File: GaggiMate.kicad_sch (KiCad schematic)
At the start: 39 parts, among them J1 Heater SSR, J10 Analog sensors, J12 BTNS, J2 Conn_01x02, J3 K-Type probe, J4 Conn_01x02, J5 Pressure Sensor, J6 Conn_01x10_Pin, J8 Conn_01x12_Pin, J9 HX711 connector, P1 USB_C_Plug_USB2.0, U1 ESP32-S3-WROOM-1, U2 MAX31855KASA, U3 ADS1115IDGS, U4 AMS1117-3.3, U5 USBLC6-2P6

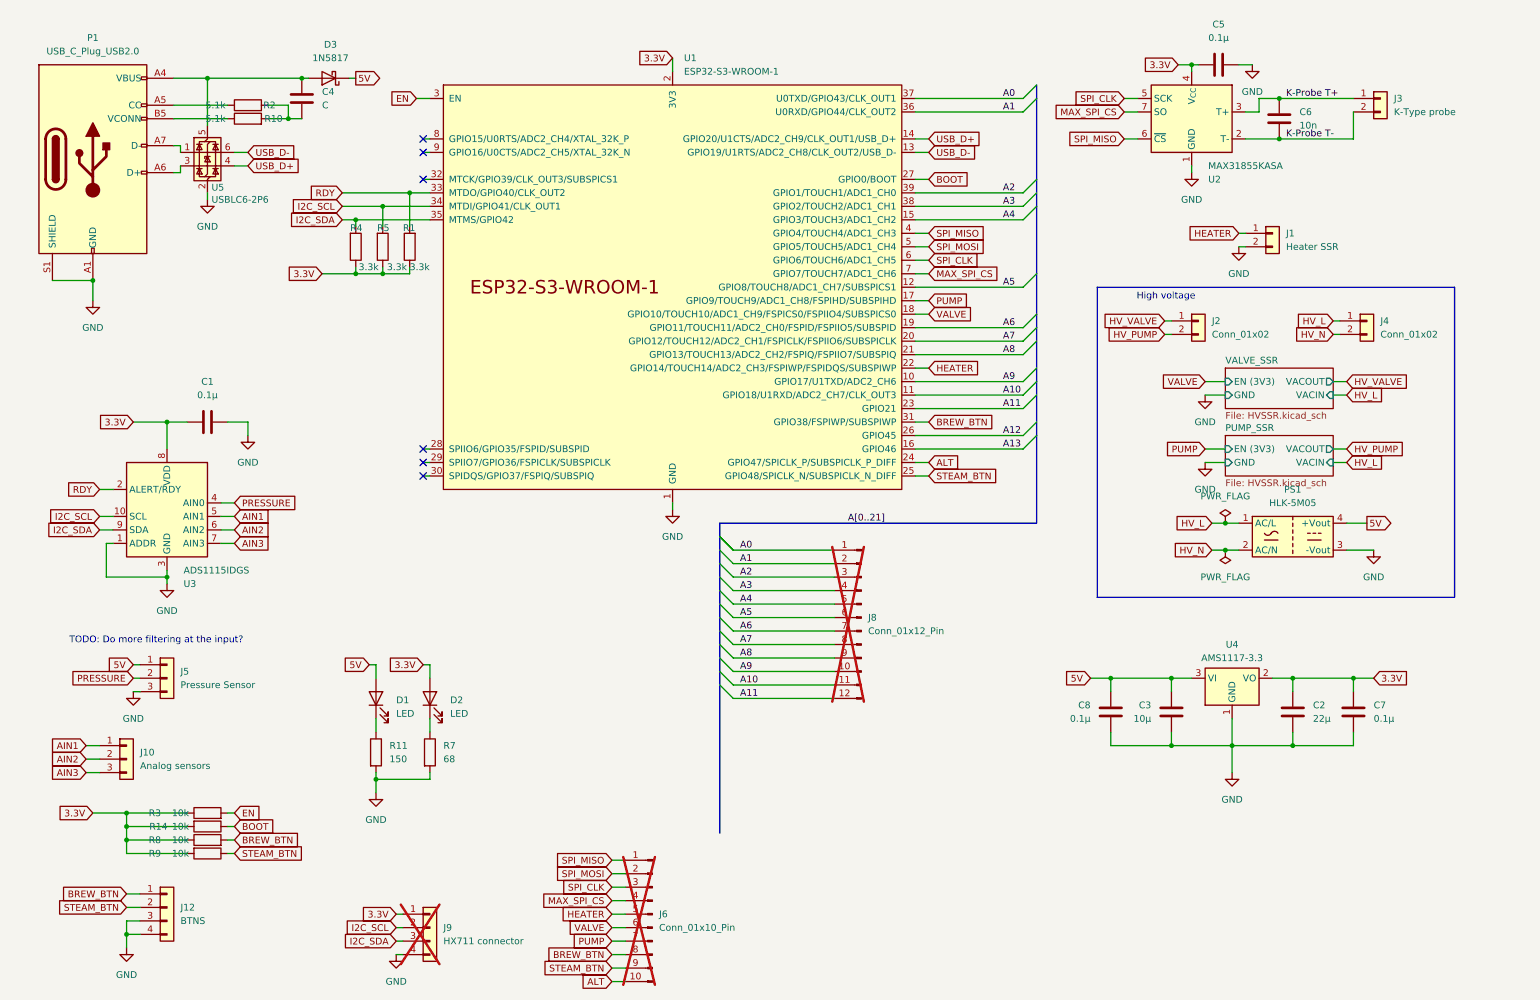
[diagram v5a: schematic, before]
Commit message: Moved front side components to other board, finished cap and resistor selection and maybe finalizing layout
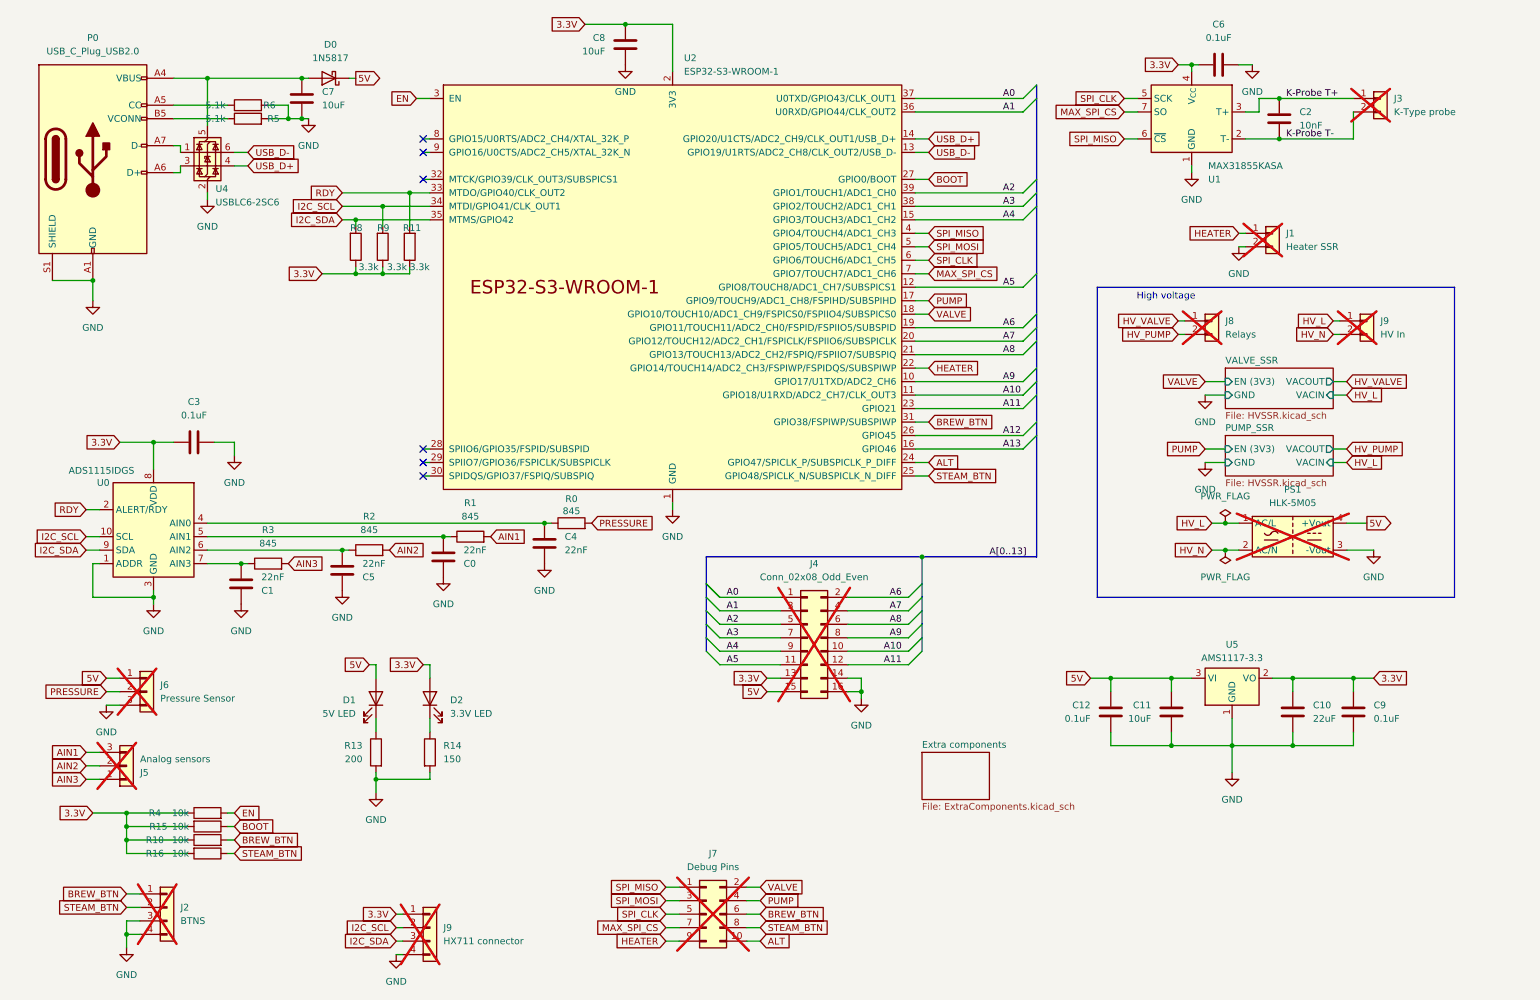
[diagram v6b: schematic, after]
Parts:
- removed J6: Conn_01x10_Pin, symbol Connector:Conn_01x10_Pin
- removed J8: Conn_01x12_Pin, Connector_PinHeader_2.54mm:PinHeader_1x12_P2.54mm_Vertical_SMD_Pin1Left, symbol Connector:Conn_01x12_Pin
- removed U5: USBLC6-2P6, Package_TO_SOT_SMD:SOT-666, symbol Power_Protection:USBLC6-2P6
- added C0, C1, C5: 22nF, Capacitor_SMD:C_0603_1608Metric, symbol Device:C
- added C7, C8: 10uF, Capacitor_SMD:C_0603_1608Metric, symbol Device:C
- added J4: Conn_02x08_Odd_Even, Connector_PinHeader_2.54mm:PinHeader_2x08_P2.54mm_Vertical_SMD, symbol Connector_Generic:Conn_02x08_Odd_Even
- added J7: Debug Pins, Connector_PinHeader_2.54mm:PinHeader_2x05_P2.54mm_Vertical_SMD, symbol Connector_Generic:Conn_02x05_Odd_Even
- added R0, R1, R2, R3: 845, Resistor_SMD:R_0603_1608Metric, symbol Device:R
- added U4: USBLC6-2SC6, Package_TO_SOT_SMD:SOT-23-6, symbol Power_Protection:USBLC6-2SC6
- C10: renamed from C2; value 22µ -> 22uF; footprint Capacitor_SMD:C_0201_0603Metric -> Capacitor_SMD:C_0603_1608Metric
- C11: renamed from C3; value 10µ -> 10uF; footprint Capacitor_SMD:C_0201_0603Metric -> Capacitor_SMD:C_0603_1608Metric
- C12: renamed from C8; value 0.1µ -> 0.1uF; footprint Capacitor_SMD:C_0201_0603Metric -> Capacitor_SMD:C_0603_1608Metric
- C2: renamed from C6; value 10n -> 10nF; footprint (none) -> Capacitor_SMD:C_0603_1608Metric
- C3: renamed from C1; value 0.1µ -> 0.1uF; footprint Capacitor_SMD:C_0201_0603Metric -> Capacitor_SMD:C_0603_1608Metric
- C4: value C -> 22nF; footprint Capacitor_SMD:C_0201_0603Metric -> Capacitor_SMD:C_0603_1608Metric
- C6: renamed from C5; value 0.1µ -> 0.1uF; footprint (none) -> Capacitor_SMD:C_0603_1608Metric
- C9: renamed from C7; value 0.1µ -> 0.1uF; footprint Capacitor_SMD:C_0201_0603Metric -> Capacitor_SMD:C_0603_1608Metric
- D1: value LED -> 5V LED; footprint (none) -> LED_SMD:LED_0603_1608Metric
- D2: value LED -> 3.3V LED; footprint (none) -> LED_SMD:LED_0603_1608Metric
- J1, J3: now not fitted
- J2: renamed from J12; now not fitted
- J5: renamed from J10; now not fitted
- J6: renamed from J5; now not fitted
- J8: renamed from J2; value Conn_01x02 -> Relays; now not fitted; now in the parts list
- J9: renamed from J4; value Conn_01x02 -> HV In; now not fitted; now in the parts list
- PS1: now not fitted; now in the parts list
- R10: renamed from R8; footprint Resistor_SMD:R_0201_0603Metric -> Resistor_SMD:R_0603_1608Metric
- R11: renamed from R1; footprint Resistor_SMD:R_0201_0603Metric -> Resistor_SMD:R_0603_1608Metric
- R13: renamed from R11; value 150 -> 200; footprint Resistor_SMD:R_0201_0603Metric -> Resistor_SMD:R_0603_1608Metric
- R14: renamed from R7; value 68 -> 150; footprint Resistor_SMD:R_0201_0603Metric -> Resistor_SMD:R_0603_1608Metric
- R15: renamed from R14; footprint Resistor_SMD:R_0201_0603Metric -> Resistor_SMD:R_0603_1608Metric
- R16: renamed from R9; footprint Resistor_SMD:R_0201_0603Metric -> Resistor_SMD:R_0603_1608Metric
- R4: renamed from R3; footprint Resistor_SMD:R_0201_0603Metric -> Resistor_SMD:R_0603_1608Metric
- R5: renamed from R10; footprint Resistor_SMD:R_0201_0603Metric -> Resistor_SMD:R_0603_1608Metric
- R6: renamed from R2; footprint Resistor_SMD:R_0201_0603Metric -> Resistor_SMD:R_0603_1608Metric
- R8: renamed from R4; footprint Resistor_SMD:R_0201_0603Metric -> Resistor_SMD:R_0603_1608Metric
- R9: renamed from R5; footprint Resistor_SMD:R_0201_0603Metric -> Resistor_SMD:R_0603_1608Metric
- renumbered D3 to D0, P1 to P0, U3 to U0, U2 to U1, U1 to U2, U4 to U5
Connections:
- net 3.3V: now also C8.2, J4.13 (Pin_13)
- net 5V: now also J4.15 (Pin_15)
- net A0: now also J4.1 (Pin_1)
- net A1: now also J4.3 (Pin_3)
- net A10: now also J4.10 (Pin_10)
- net A11: now also J4.12 (Pin_12)
- net A2: now also J4.5 (Pin_5)
- net A3: now also J4.7 (Pin_7)
- net A4: now also J4.9 (Pin_9)
- net A5: now also J4.11 (Pin_11)
- net A6: now also J4.2 (Pin_2)
- net A7: now also J4.4 (Pin_4)
- net A8: now also J4.6 (Pin_6)
- net A9: now also J4.8 (Pin_8)
- net AIN1: now also J5.3 (Pin_3), R1.2; no longer J5.1 (Pin_1), U0.5 (AIN1)
- net AIN2: now also R2.2; no longer U0.6 (AIN2)
- net AIN3: now also J5.1 (Pin_1), R3.2; no longer J5.3 (Pin_3), U0.7 (AIN3)
- net ALT: now also J7.10 (Pin_10)
- net BREW_BTN: now also J7.6 (Pin_6)
- net GND: now also C4.2, R5.2, R6.2, C0.1, C1.1, C5.1, C7.2, C8.1, J4.14 (Pin_14), J4.16 (Pin_16), U4.2 (GND)
- net HEATER: now also J7.9 (Pin_9)
- net MAX_SPI_CS: now also J7.7 (Pin_7)
- net PRESSURE: now also R0.2; no longer U0.4 (AIN0)
- net PUMP: now also J7.4 (Pin_4)
- net SPI_CLK: now also J7.5 (Pin_5)
- net SPI_MISO: now also J7.1 (Pin_1)
- net SPI_MOSI: now also J7.3 (Pin_3)
- net STEAM_BTN: now also J7.8 (Pin_8)
- net USB_D+: now also U4.4 (I/O2)
- net USB_D-: now also U4.6 (I/O1)
- net VALVE: now also J7.2 (Pin_2)
- net at D0.2 (A), P0.A4 (VBUS), P0.A9 (VBUS)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: now also C7.1, U4.5 (VBUS); no longer C4.1
- net at P0.A7 (D-): now also U4.1 (I/O1)
- net at P0.A6 (D+): now also U4.3 (I/O2)
- new net: C4.1, R0.1, U0.4 (AIN0)
- new net: C0.2, R1.1, U0.5 (AIN1)
- new net: C5.2, R2.1, U0.6 (AIN2)
- new net: C1.2, R3.1, U0.7 (AIN3)
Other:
- added sheet Extra components (ExtraComponents.kicad_sch)
- note removed: "TODO: Do more filtering at the input?"
- moved on the sheet: C3, D1, U0

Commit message: geographical referencing instead
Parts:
- renumbered C3 to C0, C2 to C1, C9 to C10, C12 to C11, C11 to C12, C4 to C2, C0 to C3, C5 to C4, C1 to C5, C10 to C9, J2 to J1, J1 to J2, J9 to J4, J9 to J8, J8 to J9, R3 to R0, R0 to R1, R11 to R10, R8 to R11, R9 to R12, R14 to R13, R15 to R14, R16 to R15, R1 to R2, R2 to R3, R6 to R5, R5 to R6, R13 to R8, R10 to R9, U5 to U6

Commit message: attempt some routing
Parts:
- renumbered J4 to J15
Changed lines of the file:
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@@
 		(dnp yes)
 		(fields_autoplaced yes)
-		(property "Reference" "J4"
+		(property "Reference" "J15"
 			(at 91.44 184.1499 0)
 			(effects
@@
 			(project ""
 				(path "/18f69721-6a2b-4a2b-8e72-291680dbbe9a"
-					(reference "J4")
+					(reference "J15")
 					(unit 1)
 				)
